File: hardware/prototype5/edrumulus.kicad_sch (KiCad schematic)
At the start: 93 parts, among them J1 Trigger Connector, J2 Raspberry Pi GPIO pins, U1 ESP32-WROOM-32U, U2 AMS1117-3.3, U3 MCP1754S-3302xMB

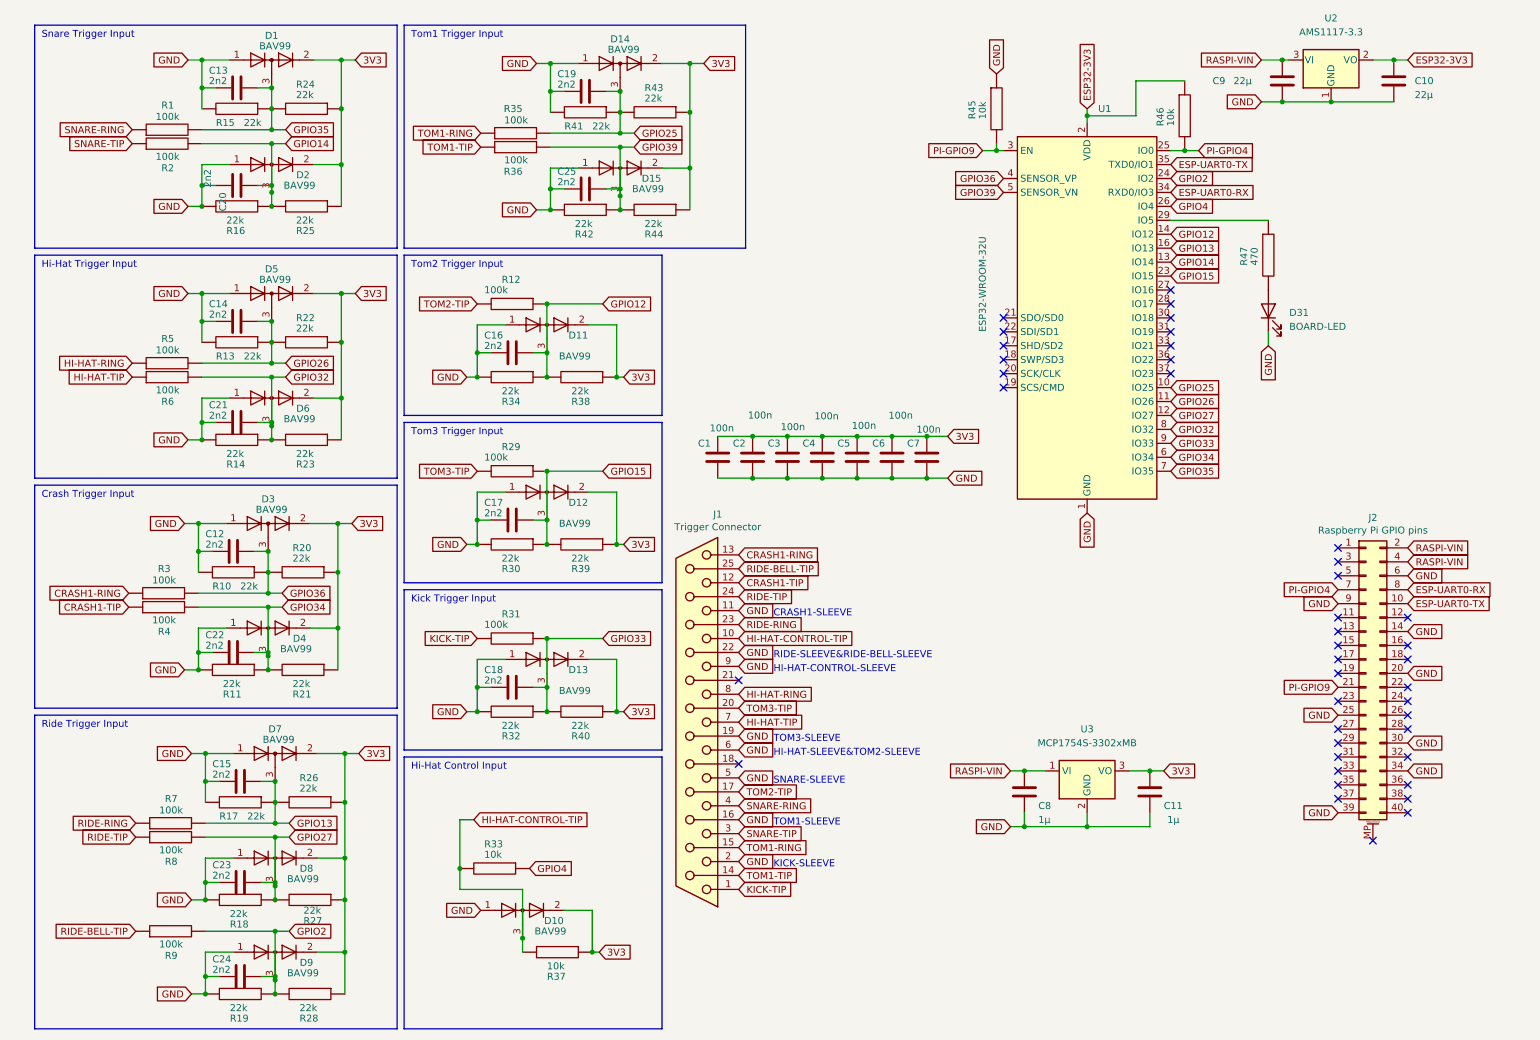
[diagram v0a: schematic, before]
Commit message: Add 3 0603 capacitors to the ESP32_3V3 net. Add one 1210 ferrite bead between RASPI-VIN and pin1 of U3. Add one 1210 ferrite bead between RASPI-VIN and pin3 of U2. Also place an 0603 cap on the RASPI-VIN side of each ferrite.
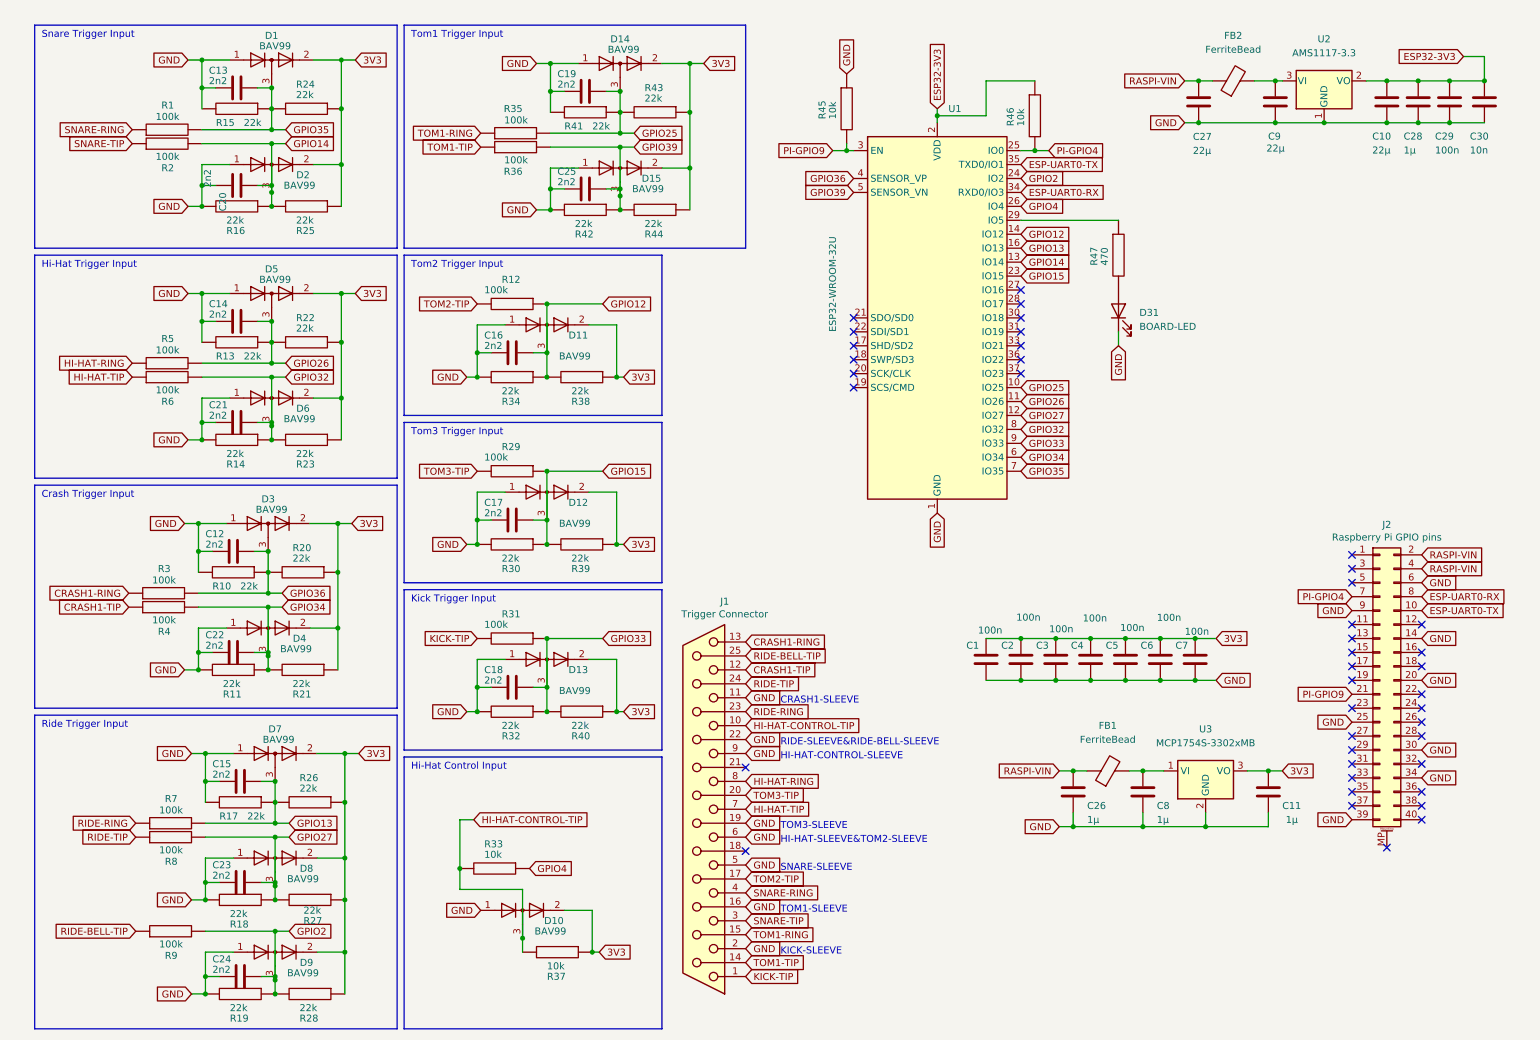
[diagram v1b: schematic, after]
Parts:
- added C26, C28: 1µ, Capacitor_SMD:C_0603_1608Metric_Pad1.08x0.95mm_HandSolder, symbol Device:C
- added C27: 22µ, Capacitor_SMD:C_0603_1608Metric_Pad1.08x0.95mm_HandSolder, symbol Device:C
- added C29: 100n, Capacitor_SMD:C_0603_1608Metric_Pad1.08x0.95mm_HandSolder, symbol Device:C
- added C30: 10n, Capacitor_SMD:C_0603_1608Metric_Pad1.08x0.95mm_HandSolder, symbol Device:C
- added FB1, FB2: FerriteBead, Inductor_SMD:L_1210_3225Metric_Pad1.42x2.65mm_HandSolder, symbol Device:FerriteBead
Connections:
- net ESP32-3V3: now also C28.1, C29.1, C30.1
- net GND: now also C26.2, C27.2, C28.2, C29.2, C30.2
- net RASPI-VIN: now also C26.1, C27.1, FB1.1, FB2.1; no longer C8.1, C9.1, U2.3 (VI), U3.1 (VI)
- new net: C8.1, FB1.2, U3.1 (VI)
- new net: C9.1, FB2.2, U2.3 (VI)
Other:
- moved on the sheet: C1, C10, C11, C2, C3, C4, C5, C6, C7, C8, C9, D31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

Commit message: delivery jstma for prototype 5 on 8/28/2022
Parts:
- J1: symbol Connector:DB25_Female -> Connector:DB25_Female_MountingHoles
- J2: footprint Connector_PinHeader_2.54mm:PinHeader_2x20_P2.54mm_Vertical -> Connector_PinSocket_2.54mm:PinSocket_2x20_P2.54mm_Vertical; symbol Connector_Generic_MountingPin:Conn_02x20_Odd_Even_MountingPin -> Connector_Generic:Conn_02x20_Odd_Even
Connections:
- net CRASH1-RING: now also R2.1; no longer R3.1
- net GPIO14: now also C12.1, D3.3 (K), R10.1, R20.2, R3.2; no longer C20.1, D2.3 (K), R16.1, R2.2, R25.2
- net GPIO36: now also C20.1, D2.3 (K), R16.1, R2.2, R25.2; no longer C12.1, D3.3 (K), R10.1, R20.2, R3.2
- net HI-HAT-RING: now also R31.2; no longer R5.1
- net HI-HAT-TIP: now also R5.1; no longer R6.1
- net KICK-TIP: now also R9.1; no longer R31.2
- net RIDE-BELL-TIP: now also R36.1; no longer R9.1
- net RIDE-RING: now also R6.1; no longer R7.1
- net RIDE-TIP: now also R1.1; no longer R8.1
- net SNARE-RING: now also R3.1; no longer R1.1
- net SNARE-TIP: now also R12.2; no longer R2.1
- net TOM1-RING: now also R7.1; no longer R35.1
- net TOM1-TIP: now also R29.2; no longer R36.1
- net TOM2-TIP: now also R8.1; no longer R12.2
- net TOM3-TIP: now also R35.1; no longer R29.2

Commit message: delivery jstma for prototype 5 on 8/28/2022 #2
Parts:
- added C31, C32, C33, C34, C35, C36, C37, C38: 100n, Capacitor_SMD:C_0603_1608Metric_Pad1.08x0.95mm_HandSolder, symbol Device:C
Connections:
- net 3V3: now also C31.1, C32.1, C33.1, C34.1, C35.1, C36.1, C37.1, C38.1
- net GND: now also C31.2, C32.2, C33.2, C34.2, C35.2, C36.2, C37.2, C38.2
- net HI-HAT-RING: now also R5.1; no longer R31.2
- net HI-HAT-TIP: now also R31.2; no longer R5.1
- net RIDE-RING: now also R35.1; no longer R6.1
- net TOM3-TIP: now also R6.1; no longer R35.1
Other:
- note added: "Bias Caps"
- note added: "GPIO 25 and 26 are DAC pins which cause an incorrect DC offset estimation and DC offset drift which makes the spike cancellation algorithm work incorrectly."
- note added: "Stitching Caps"
- moved on the sheet: C1, C12, C13, C15, C16, C17, C18, C19, C2, C20, C21, C22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

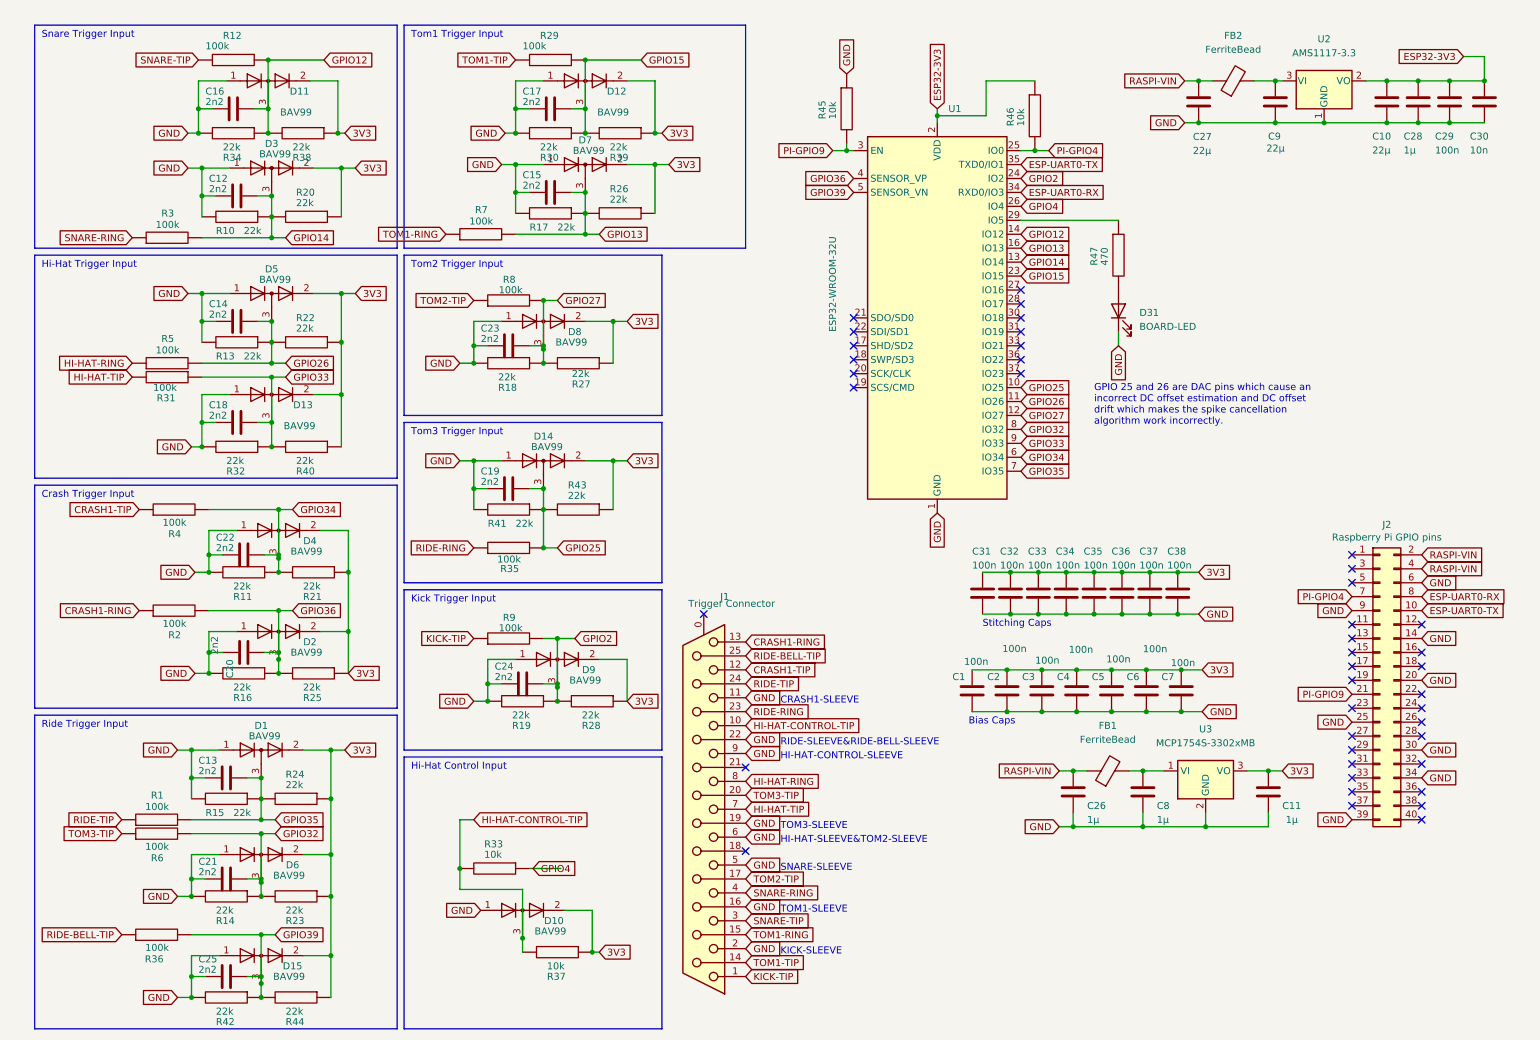
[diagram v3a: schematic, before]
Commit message: delivery jstma for prototype 5 on 8/28/2022 #3
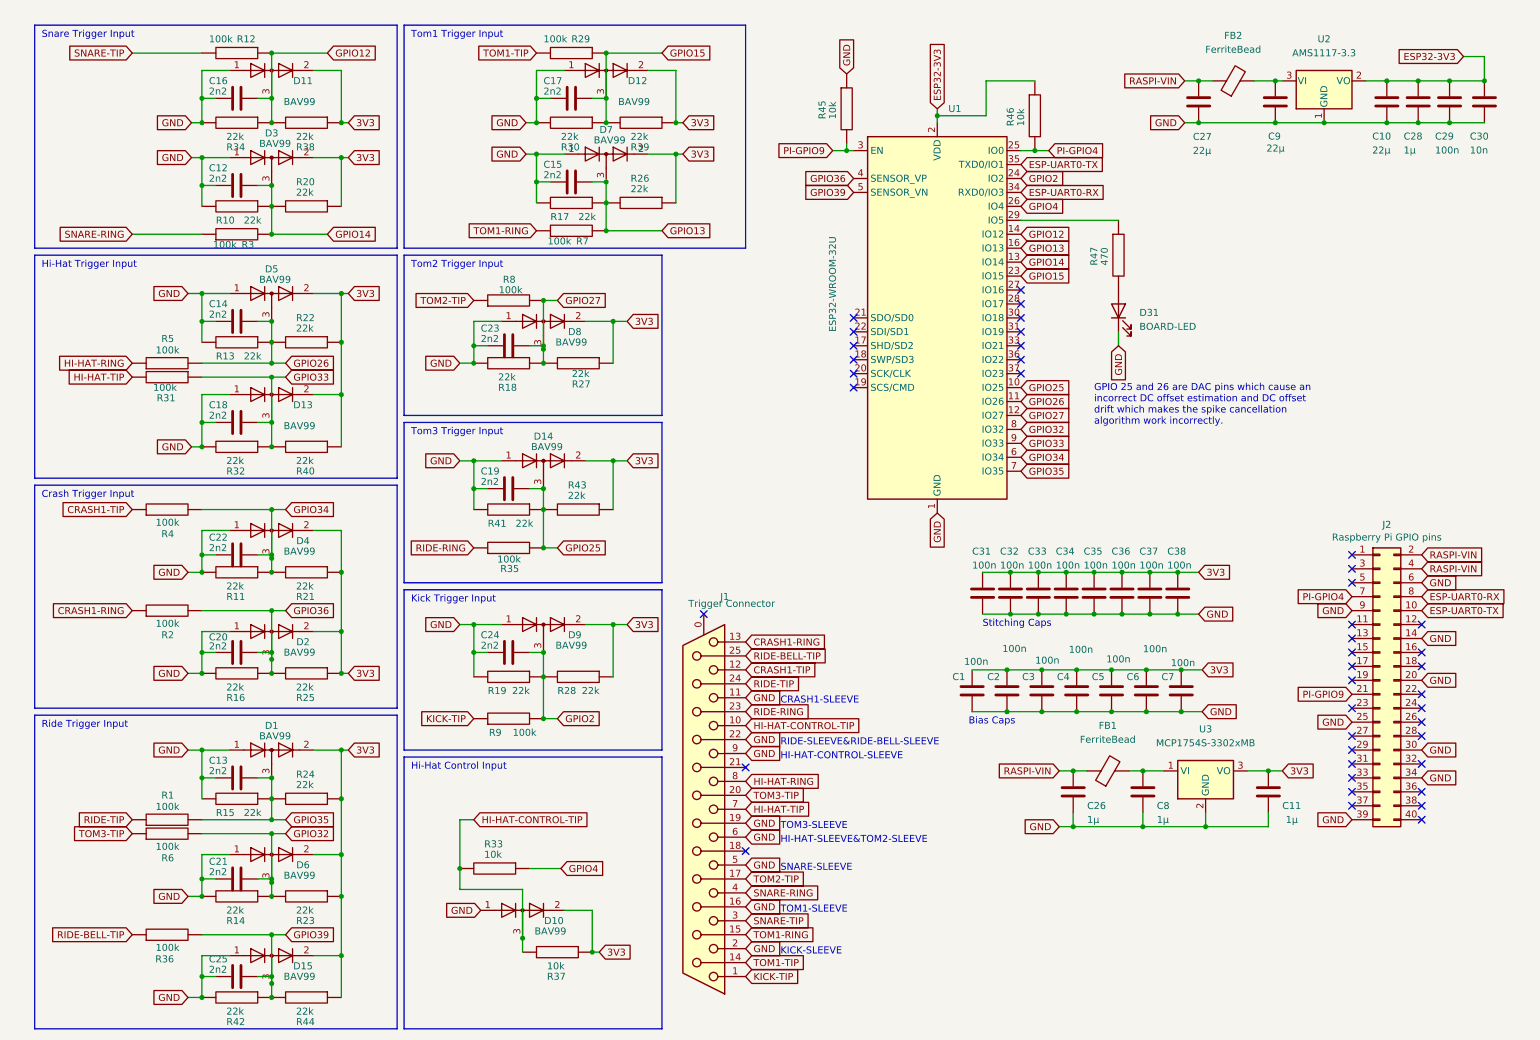
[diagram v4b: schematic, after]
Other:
- moved on the sheet: C12, C13, C15, C16, C17, C20, C21, C22, C24, C25, D1, D11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

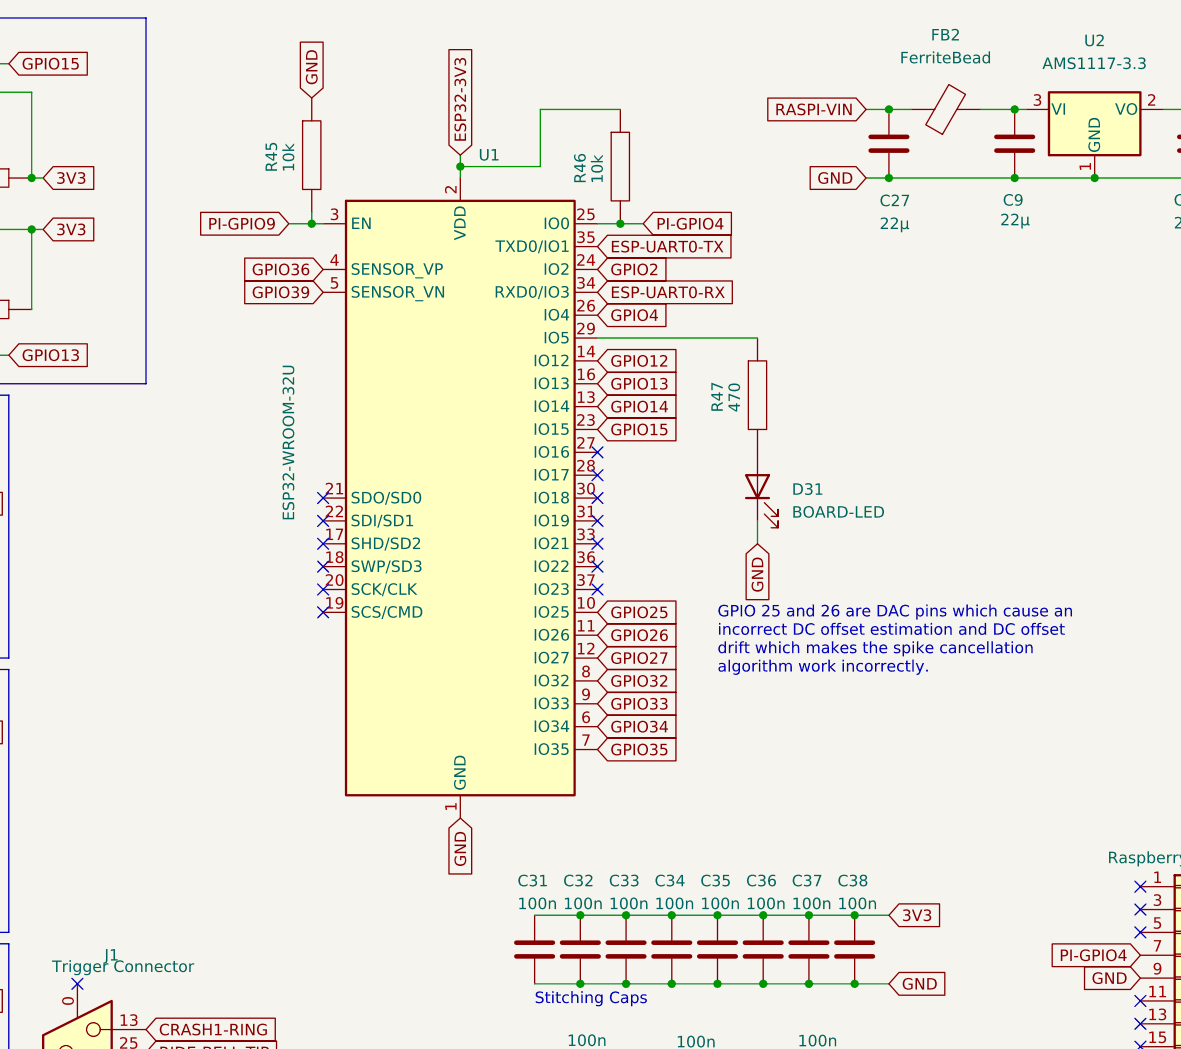
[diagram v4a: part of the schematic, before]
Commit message: change the schematics to support a GPIO board identification for prototype 5
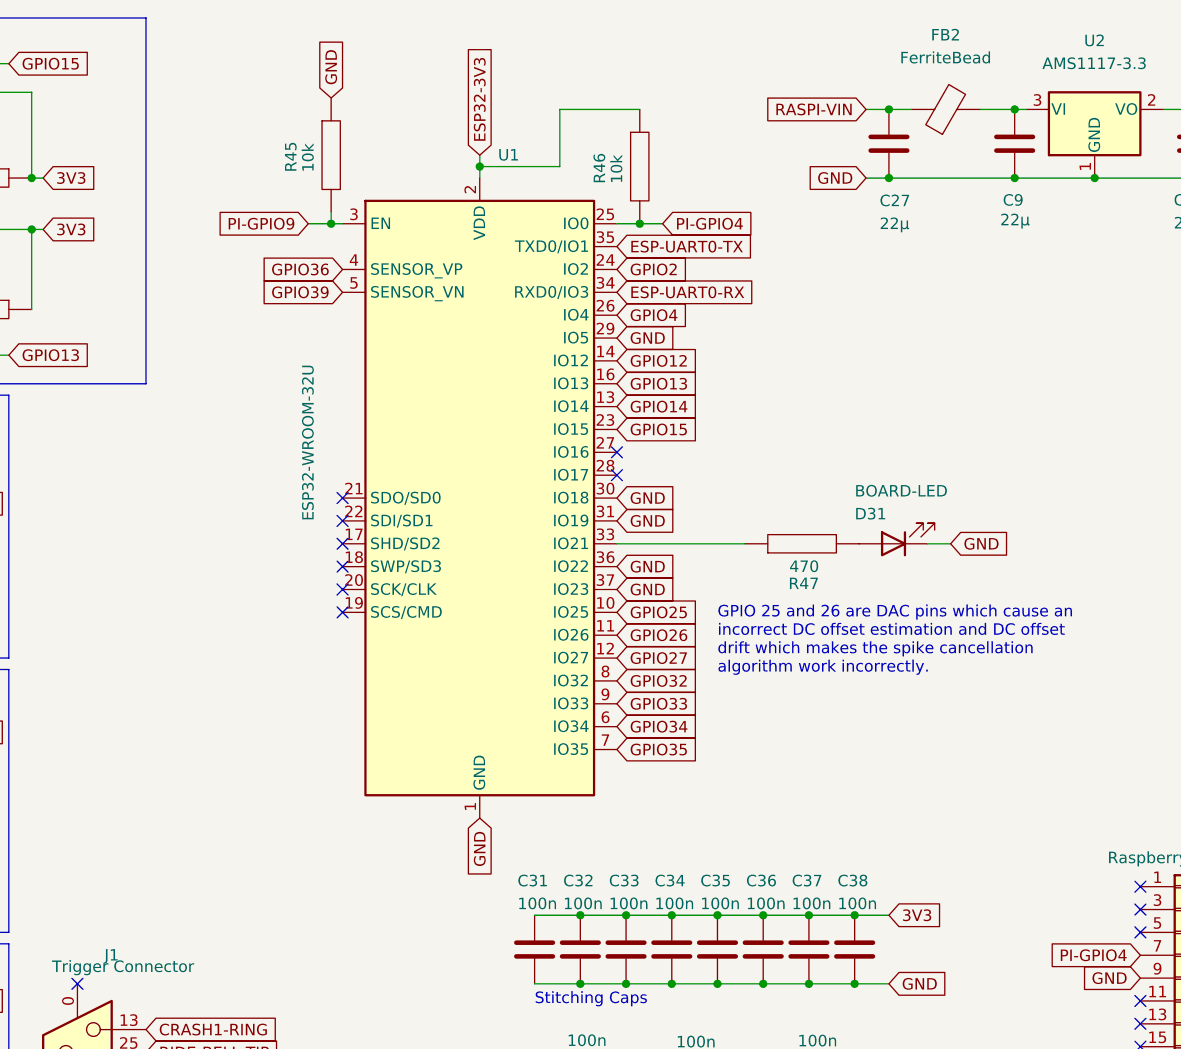
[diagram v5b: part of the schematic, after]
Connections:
- net GND: now also U1.29 (IO5), U1.30 (IO18), U1.31 (IO19), U1.36 (IO22), U1.37 (IO23)
- net at R47.1: now also U1.33 (IO21); no longer U1.29 (IO5)
- no-connect marks 42 -> 37
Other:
- moved on the sheet: D31, R45, R46, R47, U1
